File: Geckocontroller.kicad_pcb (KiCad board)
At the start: 2 copper layers, 65 parts, among them J101 AC Input, J19 I²C (BME280), J21 RGB LED, J31 DS18B20 II, J32 DS18B20 I, J40 SPI / Addon Connector, J51 USB_C_Receptacle_USB2.0, J81 Dimmer, J91 Pump, J92 HeatBed, J93 HeatLamp, K81 AQG12212, K91 AQG12112, K92 AQG12112, K93 AQG12112, Q21 AO3400A, Q222 AO3400A, Q23 AO3400A, Q51 S8050, Q52 S8050, Q81 AO3400A, Q91 AO3400A, Q92 AO3400A, Q93 AO3400A, SW1 SW_Push, U1 ESP32-WROOM-32, U101 ACT4088, U2 CP2102, U81 6N138

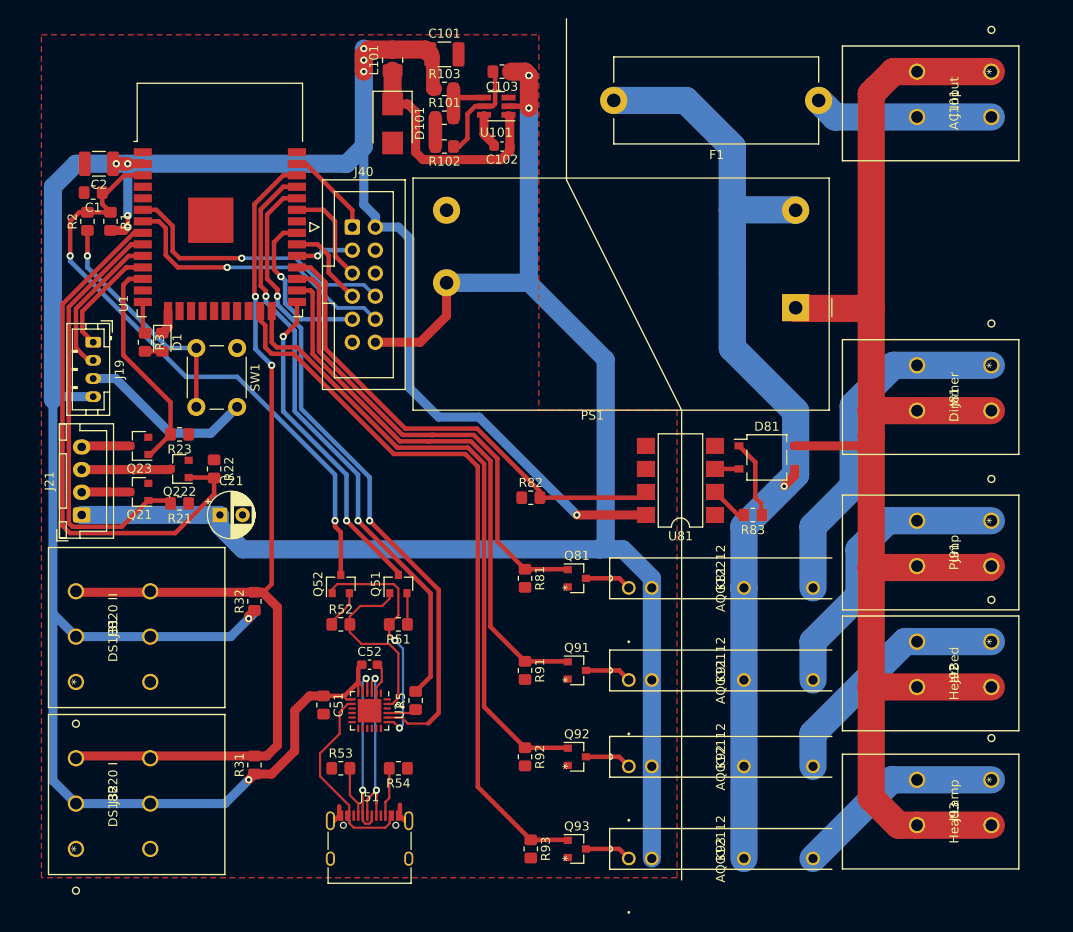
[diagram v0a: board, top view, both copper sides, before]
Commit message: PCB: Layout tweaks, ground plane for PSU
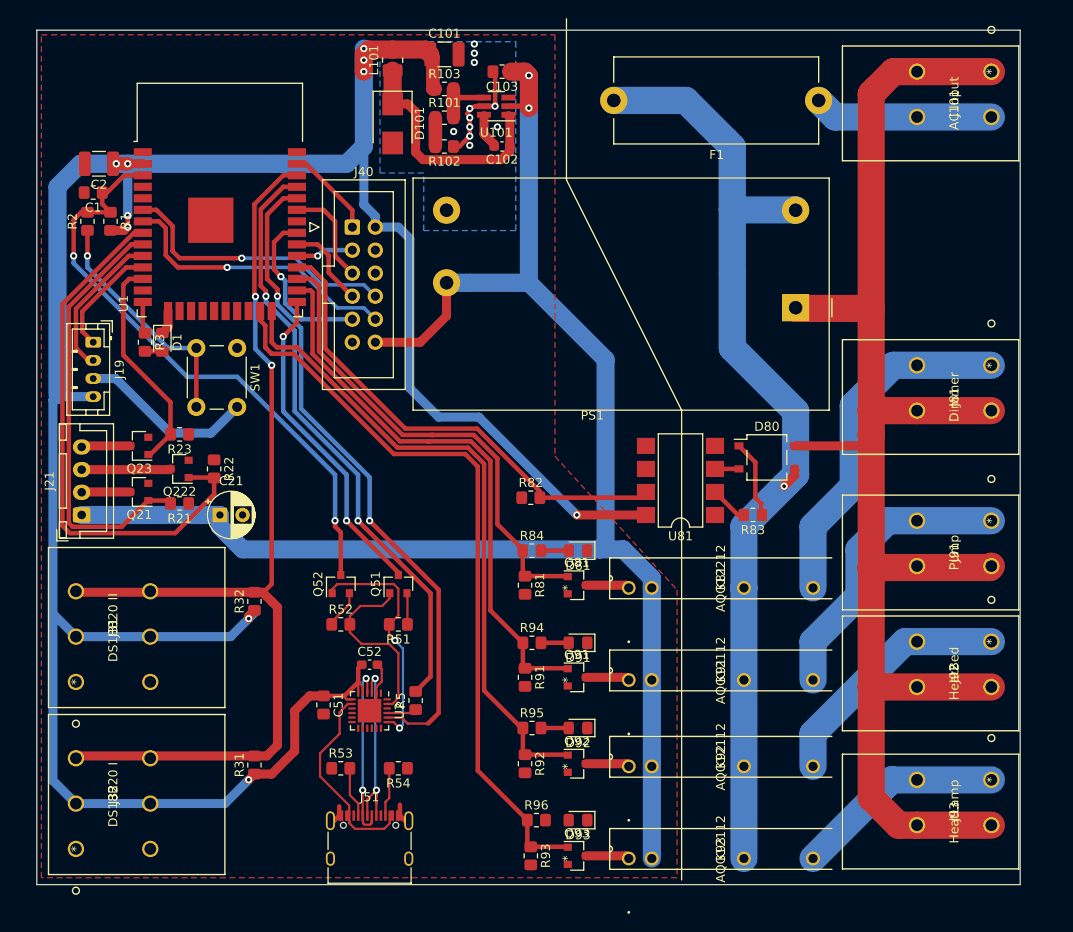
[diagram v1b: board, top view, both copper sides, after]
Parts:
- added D81: LED, LED_SMD:LED_0805_2012Metric_Pad1.15x1.40mm_HandSolder, F.Cu at (77.0, 70.6)
- added D91: LED, LED_SMD:LED_0805_2012Metric_Pad1.15x1.40mm_HandSolder, F.Cu at (77.0, 80.8)
- added D92: LED, LED_SMD:LED_0805_2012Metric_Pad1.15x1.40mm_HandSolder, F.Cu at (77.0, 90.2)
- added D93: LED, LED_SMD:LED_0805_2012Metric_Pad1.15x1.40mm_HandSolder, F.Cu at (77.0, 100.3)
- added R84: 220R, Resistor_SMD:R_0805_2012Metric_Pad1.20x1.40mm_HandSolder, F.Cu at (71.9, 70.6)
- added R94: 470R, Resistor_SMD:R_0805_2012Metric_Pad1.20x1.40mm_HandSolder, F.Cu at (71.9, 80.8)
- added R95: 470R, Resistor_SMD:R_0805_2012Metric_Pad1.20x1.40mm_HandSolder, F.Cu at (71.9, 90.2)
- added R96: 470R, Resistor_SMD:R_0805_2012Metric_Pad1.20x1.40mm_HandSolder, F.Cu at (72.4, 100.3)
- moved Q81 0.76 mm to (76.8, 74.4)
- moved Q91 0.76 mm to (76.8, 84.6)
- moved Q92 0.76 mm to (76.8, 94.1)
- moved Q93 0.76 mm to (76.8, 104.3)
- moved R81 0.76 mm to (71.1, 74.4)
- moved R91 0.76 mm to (71.1, 84.6)
- moved R92 0.76 mm to (71.1, 94.1)
- moved R93 0.76 mm to (71.8, 104.3)
- renumbered D81 to D80
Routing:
- net Net-(D92-Pad2): track 0.00 -> 3.05 mm
- net Net-(D91-Pad2): track 0.00 -> 3.05 mm
- net Net-(D81-Pad2): track 0.00 -> 3.05 mm
- net /Relay1_out: track 61.7 -> 63.0 mm
- net +3V3: track 280.9 -> 279.9 mm
- net /Relay2_out: track 70.4 -> 71.2 mm
- net /Dimmer_out: track 53.1 -> 53.9 mm
- net /Relay3_out: track 80.8 -> 81.6 mm
- net EN: track 67.3 -> 66.8 mm
- net GND: track 44.5 -> 44.9 mm, vias 0 -> 11
- added copper zone on B.Cu, net GND
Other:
- board outline added: 108.5 x 94.2 mm

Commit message: PCB: Re-arrange PSU parts
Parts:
- moved C101 11.3 mm to (65.5, 26.7)
- moved L101 11.3 mm to (65.3, 23.6), turned to 180 degrees
- moved C102 6.70 mm to (65.5, 20.1)
- moved R102 6.49 mm to (59.7, 20.1), turned to 0 degrees
- moved R101 5.98 mm to (61.0, 17.0), turned to 90 degrees
- moved U101 5.36 mm to (65.2, 17.0)
- moved R103 4.86 mm to (58.2, 17.0), turned to 90 degrees
- moved D101 2.67 mm to (59.2, 23.6), turned to 180 degrees
- moved C103 0.25 mm to (68.6, 18.0), turned to 270 degrees
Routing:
- net (no net): track 0.00 -> 13.8 mm, vias 0 -> 6
- net Net-(C102-Pad1): track 26.1 -> 14.4 mm
- net +3V3: track 279.9 -> 289.3 mm, vias 10 -> 17
- net +12V: track 209.2 -> 214.8 mm, vias 3 -> 0
- net GND: track 44.9 -> 40.2 mm, vias 11 -> 13
- net Net-(C102-Pad2): track 3.88 -> 2.46 mm
- net Net-(R101-Pad1): track 3.18 -> 2.16 mm
- net Net-(R101-Pad2): track 6.56 -> 5.66 mm

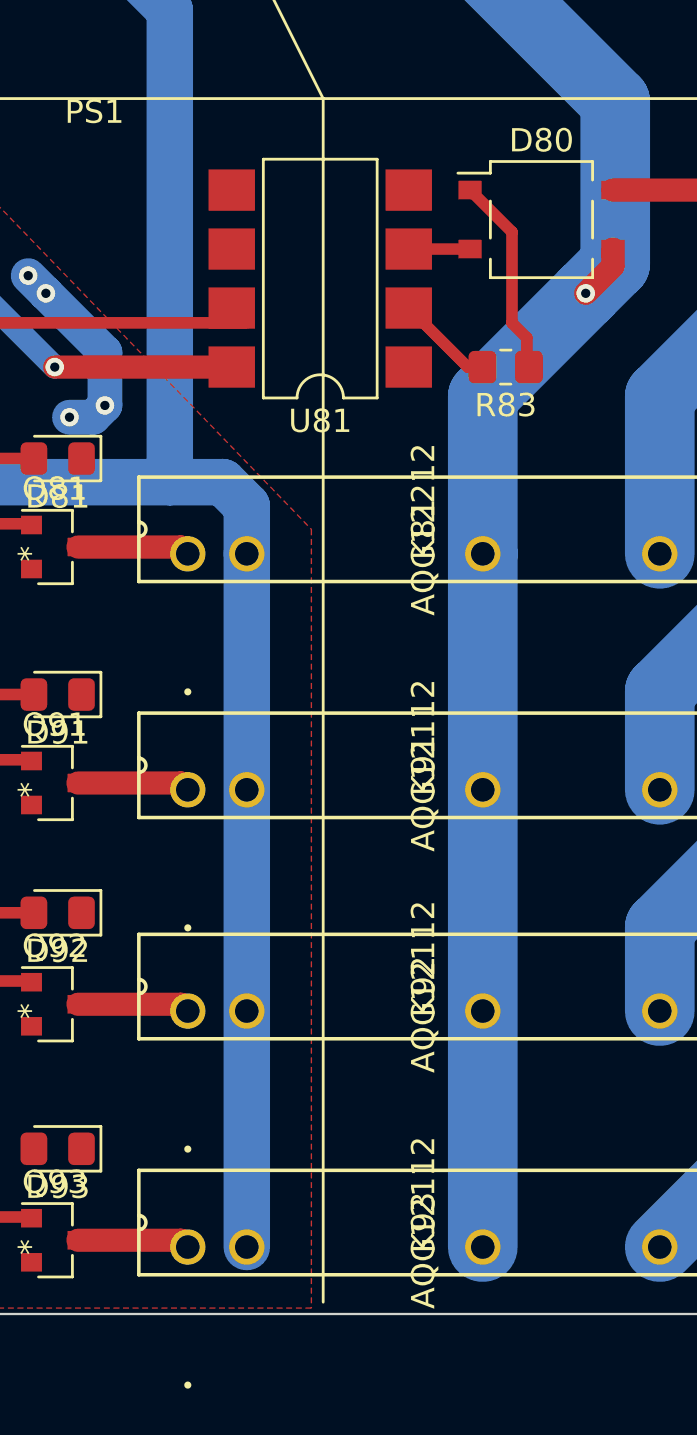
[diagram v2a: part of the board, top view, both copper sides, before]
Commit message: Schema: Cutout millings
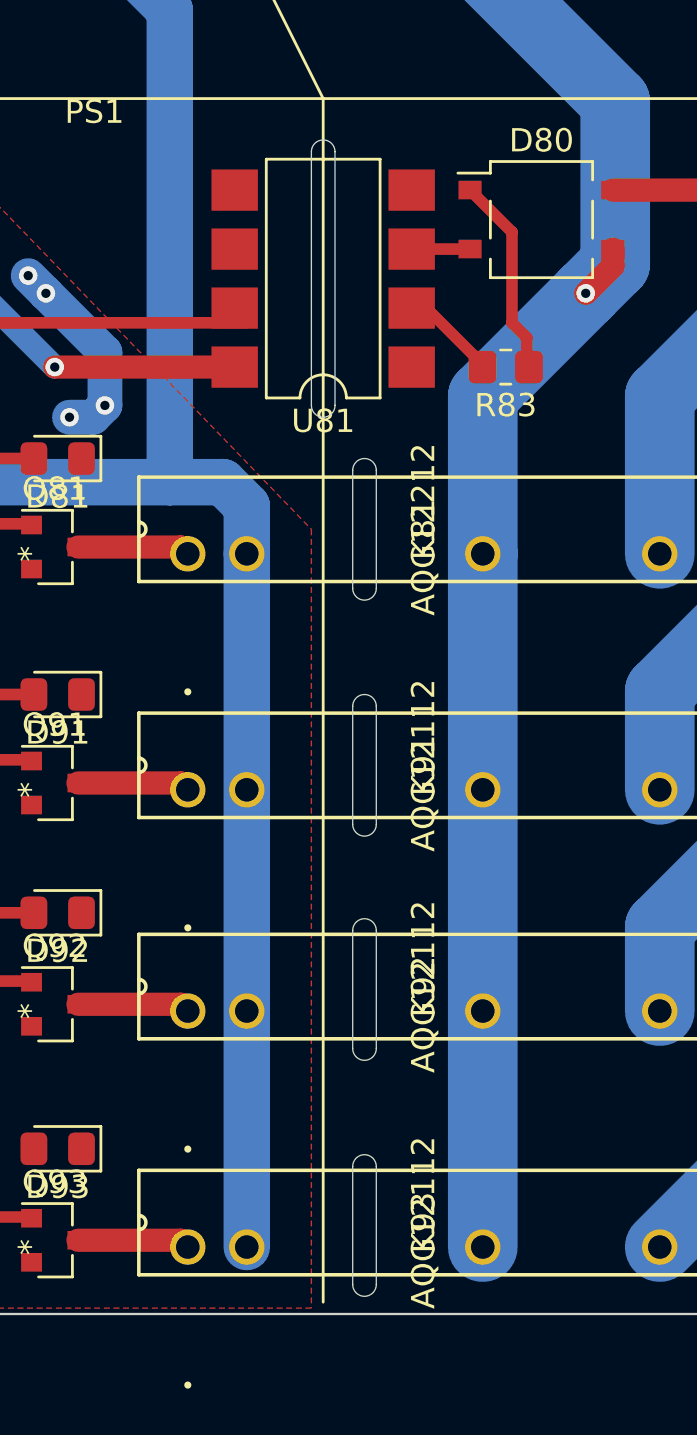
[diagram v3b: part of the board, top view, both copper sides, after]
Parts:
- moved U81 0.13 mm to (88.4, 62.9)
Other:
- outline, holes or cut-outs redrawn
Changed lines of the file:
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@@
   (general
     (thickness 1.6)
-    (drawings 4)
-    (tracks 604)
+    (drawings 24)
+    (tracks 605)
     (zones 0)
     (modules 73)
@@
     (pad_to_mask_clearance 0)
     (aux_axis_origin 0 0)
-    (visible_elements FFFFFF7F)
+    (visible_elements FFF9FF7F)
     (pcbplotparams
       (layerselection 0x010fc_ffffffff)
@@
   )
   (module Package_DIP:SMDIP-8_W7.62mm (layer F.Cu)
-    (at 88.265 62.865 180)
+    (at 88.392 62.865 180)
     (descr "8-lead surface-mounted (SMD) DIP package, row spacing 7.62 mm (300 mils)")
     (tags "SMD DIP DIL PDIP SMDIP 2.54mm 7.62mm 300mil")
@@
     )
   )
+  (gr_arc (start 90.17 101.092) (end 90.678 101.092) (angle -180) (layer Edge.Cuts) (width 0.05))
+  (gr_arc (start 90.17 106.172) (end 89.662 106.172) (angle -180) (layer Edge.Cuts) (width 0.05))
+  (gr_line (start 89.662 101.092) (end 89.662 106.172) (layer Edge.Cuts) (width 0.05))
+  (gr_line (start 90.678 106.172) (end 90.678 101.092) (layer Edge.Cuts) (width 0.05))
+  (gr_arc (start 90.17 90.932) (end 90.678 90.932) (angle -180) (layer Edge.Cuts) (width 0.05))
+  (gr_arc (start 90.17 96.012) (end 89.662 96.012) (angle -180) (layer Edge.Cuts) (width 0.05))
+  (gr_line (start 90.678 96.012) (end 90.678 90.932) (layer Edge.Cuts) (width 0.05))
+  (gr_line (start 89.662 90.932) (end 89.662 96.012) (layer Edge.Cuts) (width 0.05))
+  (gr_arc (start 90.17 81.28) (end 90.678 81.28) (angle -180) (layer Edge.Cuts) (width 0.05))
+  (gr_line (start 90.678 86.36) (end 90.678 81.28) (layer Edge.Cuts) (width 0.05))
+  (gr_line (start 89.662 81.28) (end 89.662 86.36) (layer Edge.Cuts) (width 0.05))
+  (gr_arc (start 90.17 86.36) (end 89.662 86.36) (angle -180) (layer Edge.Cuts) (width 0.05))
+  (gr_line (start 89.662 71.12) (end 89.662 76.2) (layer Edge.Cuts) (width 0.05))
+  (gr_arc (start 90.17 76.2) (end 89.662 76.2) (angle -180) (layer Edge.Cuts) (width 0.05))
+  (gr_arc (start 90.17 71.12) (end 90.678 71.12) (angle -180) (layer Edge.Cuts) (width 0.05))
+  (gr_line (start 90.678 76.2) (end 90.678 71.12) (layer Edge.Cuts) (width 0.05))
+  (gr_arc (start 88.392 68.326) (end 87.884 68.326) (angle -180) (layer Edge.Cuts) (width 0.05))
+  (gr_arc (start 88.392 57.404) (end 88.9 57.404) (angle -180) (layer Edge.Cuts) (width 0.05))
+  (gr_line (start 88.9 68.326) (end 88.9 57.404) (layer Edge.Cuts) (width 0.05))
+  (gr_line (start 87.884 57.404) (end 87.884 68.326) (layer Edge.Cuts) (width 0.05))
   (gr_poly (pts (xy 125.73 107.442) (xy 17.272 107.442) (xy 17.272 13.208) (xy 125.73 13.208)) (layer Edge.Cuts) (width 0.1))
   (gr_line (start 88.392 55.118) (end 88.392 106.934) (layer F.SilkS) (width 0.12))
@@
   (segment (start 28.965 46.38) (end 29.21 46.625) (width 0.5) (layer F.Cu) (net 28))
   (segment (start 28.965 43.18) (end 28.965 46.38) (width 0.5) (layer F.Cu) (net 28))
+  (segment (start 92.837 64.135) (end 92.075 64.135) (width 0.5) (layer F.Cu) (net 29))
+  (segment (start 95.25 66.548) (end 92.837 64.135) (width 0.5) (layer F.Cu) (net 29))
+  (segment (start 95.25 66.675) (end 95.25 66.548) (width 0.5) (layer F.Cu) (net 29))
   (segment (start 72.755 64.77) (end 85.09 64.77) (width 0.5) (layer F.Cu) (net 41))
   (segment (start 72.755 64.66) (end 72.755 64.77) (width 0.5) (layer F.Cu) (net 41))
-  (segment (start 94.615 66.675) (end 92.075 64.135) (width 0.5) (layer F.Cu) (net 29))
-  (segment (start 95.25 66.675) (end 94.615 66.675) (width 0.5) (layer F.Cu) (net 29))
   (segment (start 61.01 16.068) (end 60.96 16.018) (width 0.6) (layer F.Cu) (net 30))
   (segment (start 63.801 16.068) (end 61.01 16.068) (width 0.6) (layer F.Cu) (net 30))

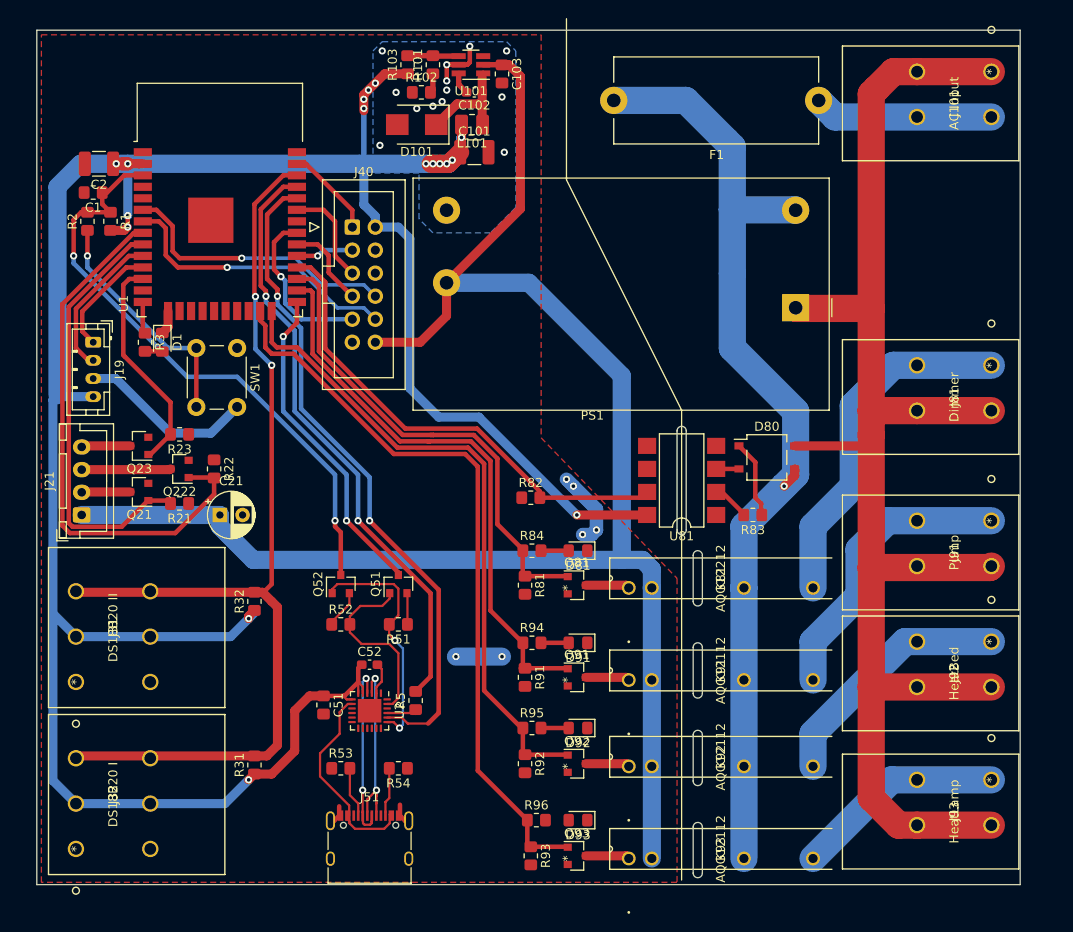
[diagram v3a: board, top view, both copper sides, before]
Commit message: PCB: Add HX711 load cell input + PWM fan connector
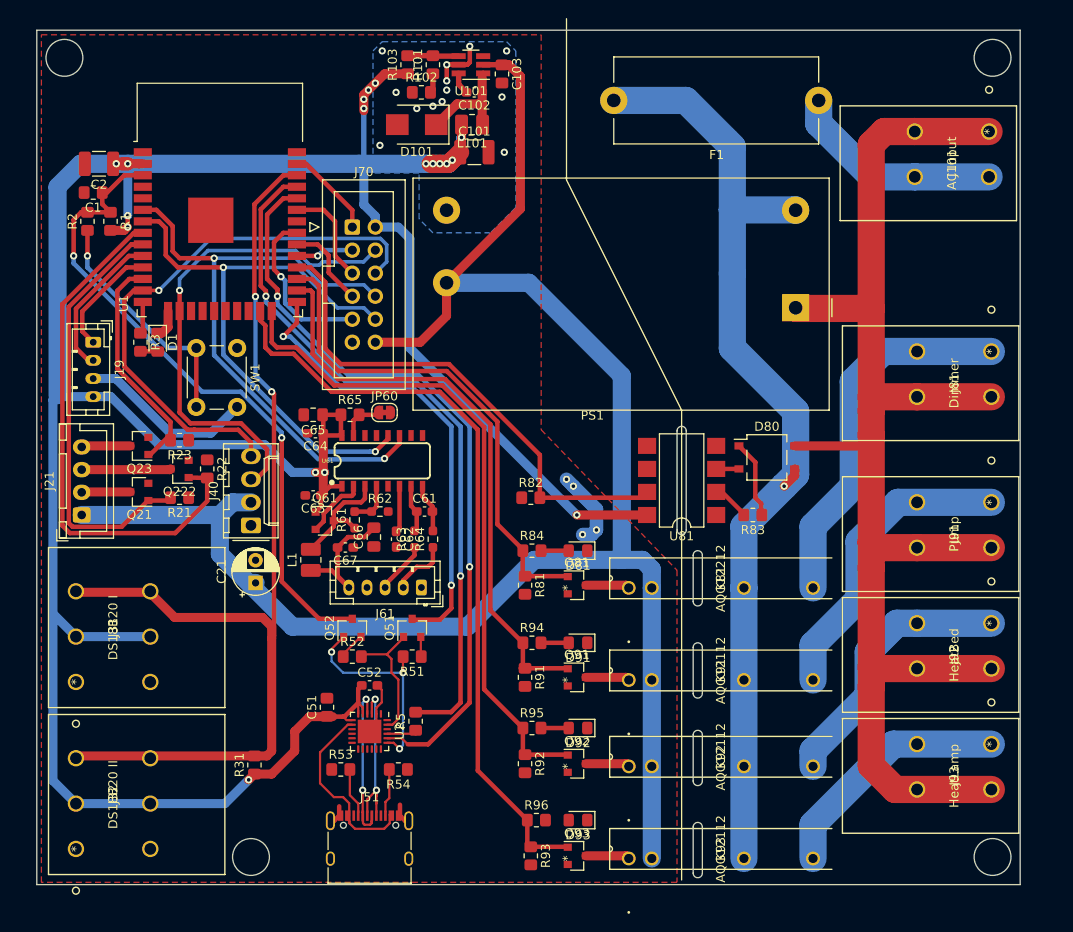
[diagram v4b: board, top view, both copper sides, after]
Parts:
- removed R32: 4k7, Resistor_SMD:R_0805_2012Metric_Pad1.20x1.40mm_HandSolder
- added C61: 100nF, Capacitor_SMD:C_0603_1608Metric_Pad1.08x0.95mm_HandSolder, F.Cu at (60.0, 66.3)
- added C62: 100nF, Capacitor_SMD:C_0603_1608Metric_Pad1.08x0.95mm_HandSolder, F.Cu at (56.9, 69.3)
- added C63: 100nF, Capacitor_SMD:C_0603_1608Metric_Pad1.08x0.95mm_HandSolder, F.Cu at (47.8, 64.5)
- added C64: 100nF, Capacitor_SMD:C_0603_1608Metric_Pad1.08x0.95mm_HandSolder, F.Cu at (48.0, 57.7)
- added C65: 10µF, Capacitor_SMD:C_0805_2012Metric_Pad1.18x1.45mm_HandSolder, F.Cu at (47.8, 55.6)
- added C66: 10µF, Capacitor_SMD:C_0805_2012Metric_Pad1.18x1.45mm_HandSolder, F.Cu at (54.4, 69.1)
- added C67: 100nF, Capacitor_SMD:C_0603_1608Metric_Pad1.08x0.95mm_HandSolder, F.Cu at (51.3, 70.3)
- added J40: Fan Connector, Connector_Molex:Molex_KK-254_AE-6410-04A_1x04_P2.54mm_Vertical, F.Cu at (40.9, 67.8)
- added J61: Load Cell Connector, Connector_JST:JST_PH_B5B-PH-K_1x05_P2.00mm_Vertical, F.Cu at (59.7, 74.7)
- added JP60: Jumper, Jumper:SolderJumper-2_P1.3mm_Bridged_RoundedPad1.0x1.5mm, F.Cu at (55.6, 55.4)
- added L1: 3.3µH, Inductor_SMD:L_1008_2520Metric_Pad1.43x2.20mm_HandSolder, F.Cu at (47.5, 71.6)
- added Q61: S8550, Package_TO_SOT_SMD:SOT-23, F.Cu at (49.0, 67.3)
- added R61: R, Resistor_SMD:R_0603_1608Metric_Pad0.98x0.95mm_HandSolder, F.Cu at (52.3, 67.2)
- added R62: R, Resistor_SMD:R_0603_1608Metric_Pad0.98x0.95mm_HandSolder, F.Cu at (55.1, 66.3)
- added R63: 100R, Resistor_SMD:R_0603_1608Metric_Pad0.98x0.95mm_HandSolder, F.Cu at (58.9, 69.3)
- added R64: 100R, Resistor_SMD:R_0603_1608Metric_Pad0.98x0.95mm_HandSolder, F.Cu at (61.0, 69.3)
- added R65: 10k, Resistor_SMD:R_0805_2012Metric_Pad1.20x1.40mm_HandSolder, F.Cu at (51.8, 55.6)
- added U61: HX711, footprints:SO16, F.Cu at (55.4, 60.7)
- J31: value DS18B20 II -> DS18B20 I
- J32: value DS18B20 I -> DS18B20 II
- R84: value 220R -> 470R
- moved C21 8.46 mm to (41.4, 74.2), turned to 90 degrees
- moved J101 6.61 mm to (122.3, 24.4)
- moved Q51 5.06 mm to (58.7, 79.1)
- moved Q52 4.99 mm to (52.1, 79.1)
- moved J93 3.94 mm to (122.6, 91.9)
- moved R51 3.87 mm to (58.7, 82.3)
- moved R52 3.78 mm to (52.1, 82.3)
- moved C52 2.29 mm to (54.0, 85.5)
- moved R5 2.29 mm to (59.1, 89.4)
- moved U2 2.29 mm to (54.0, 90.6)
- moved J91 2.03 mm to (122.6, 65.3)
- moved J92 2.03 mm to (122.6, 78.6)
- moved J81 1.52 mm to (122.6, 48.6)
- moved R22 0.76 mm to (36.1, 61.6)
- moved R21 0.64 mm to (33.0, 64.8)
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- renumbered J40 to J70
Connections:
- net GPIO34 renamed HX_CLK
- net GPIO35 renamed HX_DATA
- J70 pad 4: (no net) -> FAN_SIG
- J70 pad 6: (no net) -> FAN_PWM
- U1 pad 13: (no net) -> FAN_PWM
- U1 pad 16: (no net) -> FAN_SIG
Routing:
- net FAN_PWM: track 0.00 -> 62.7 mm, vias 0 -> 1
- net FAN_SIG: track 0.00 -> 55.3 mm, vias 0 -> 1
- net HX_CLK: track 31.9 -> 68.9 mm, vias 1 -> 2
- net +3V3: track 289.3 -> 322.1 mm, vias 17 -> 18
- net HX_DATA: track 31.9 -> 64.5 mm, vias 1 -> 2
- net IO0: track 36.0 -> 52.0 mm
- net /E+: track 0.00 -> 14.8 mm
- net (no net): track 13.8 -> 0.00 mm, vias 6 -> 0
- net /AVDD: track 0.00 -> 12.9 mm
- net +12V: track 214.8 -> 227.3 mm
- net /TXD': track 66.6 -> 78.5 mm
- net /N: track 163.5 -> 153.8 mm
- net RXD: track 73.3 -> 83.0 mm
- net GND: track 40.2 -> 48.9 mm, vias 13 -> 17
- net Net-(Q61-Pad2): track 0.00 -> 7.16 mm
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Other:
- outline, holes or cut-outs redrawn
